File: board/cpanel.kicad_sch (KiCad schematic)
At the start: 12 parts, among them J18 LCD, SW11 RI, SW12 UP, SW13 LE, SW14 OK, SW15 DN, SW16 CANCEL, SW17 BACK, SW18 MENU, U19 BOB-12009, U20 MCP23008-xP

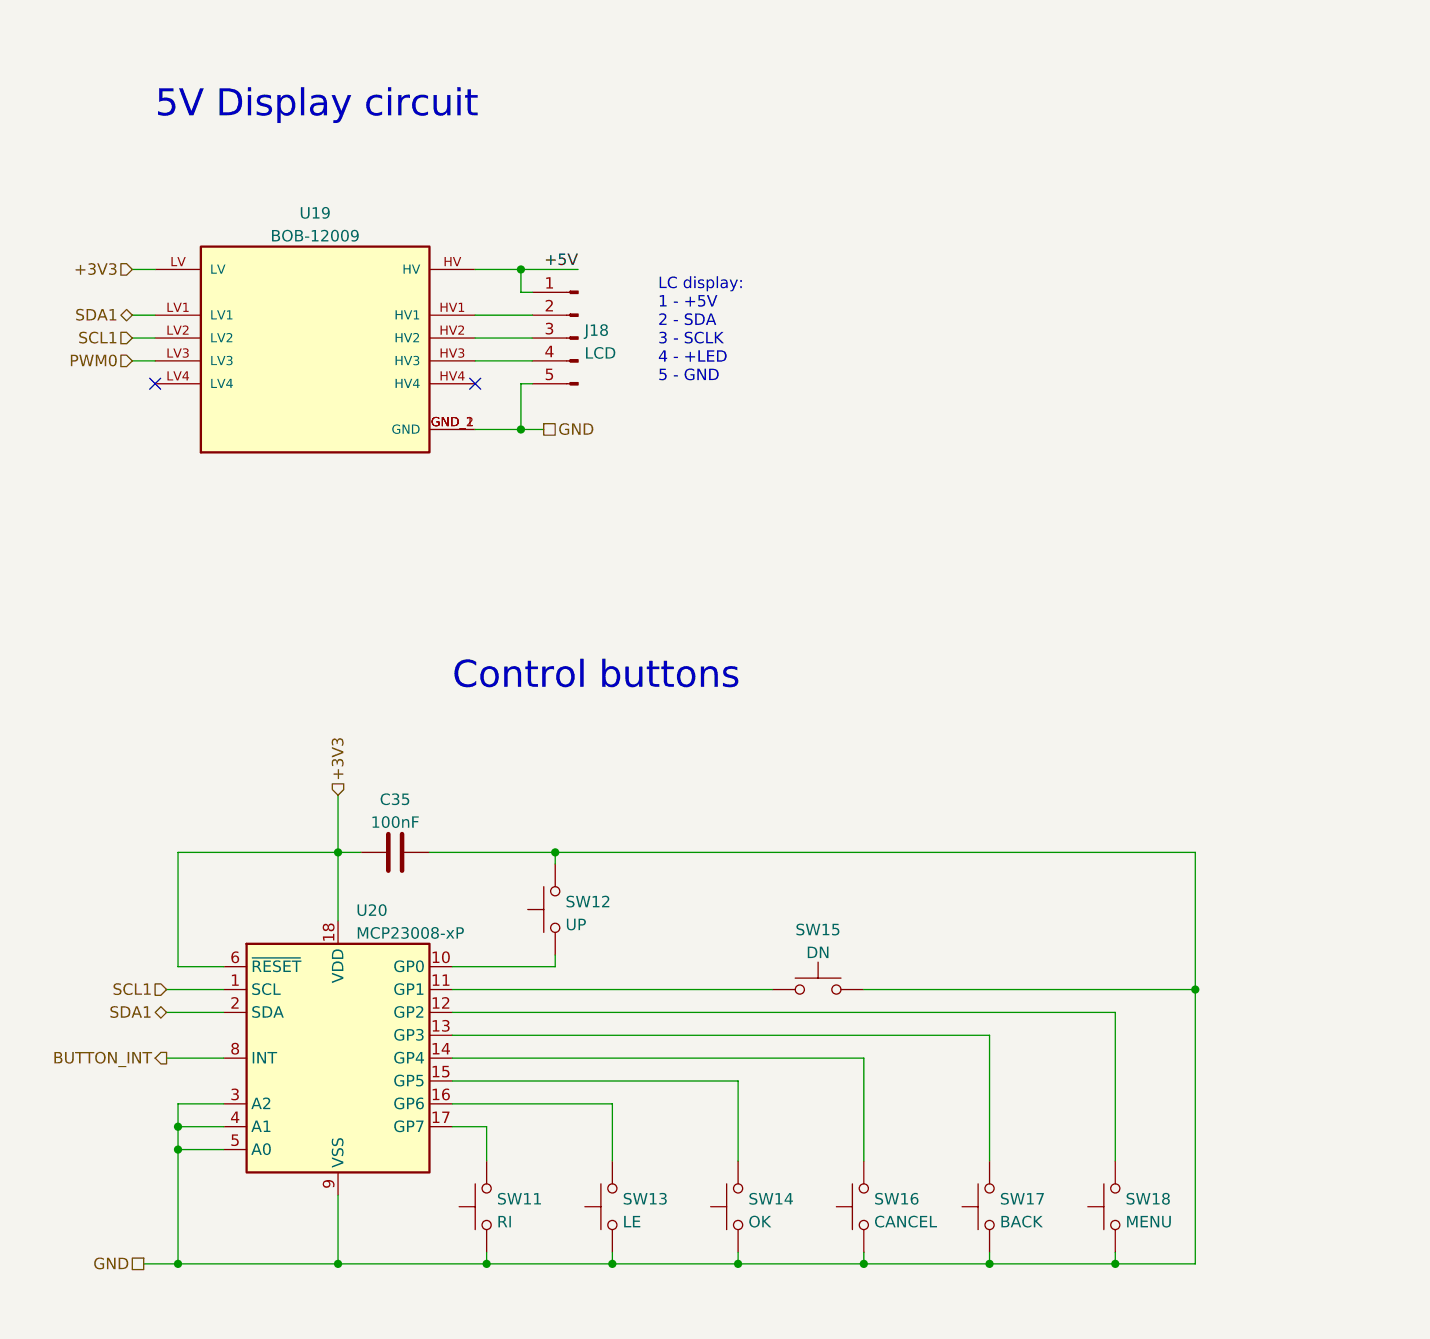
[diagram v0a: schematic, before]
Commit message: Modularize board.
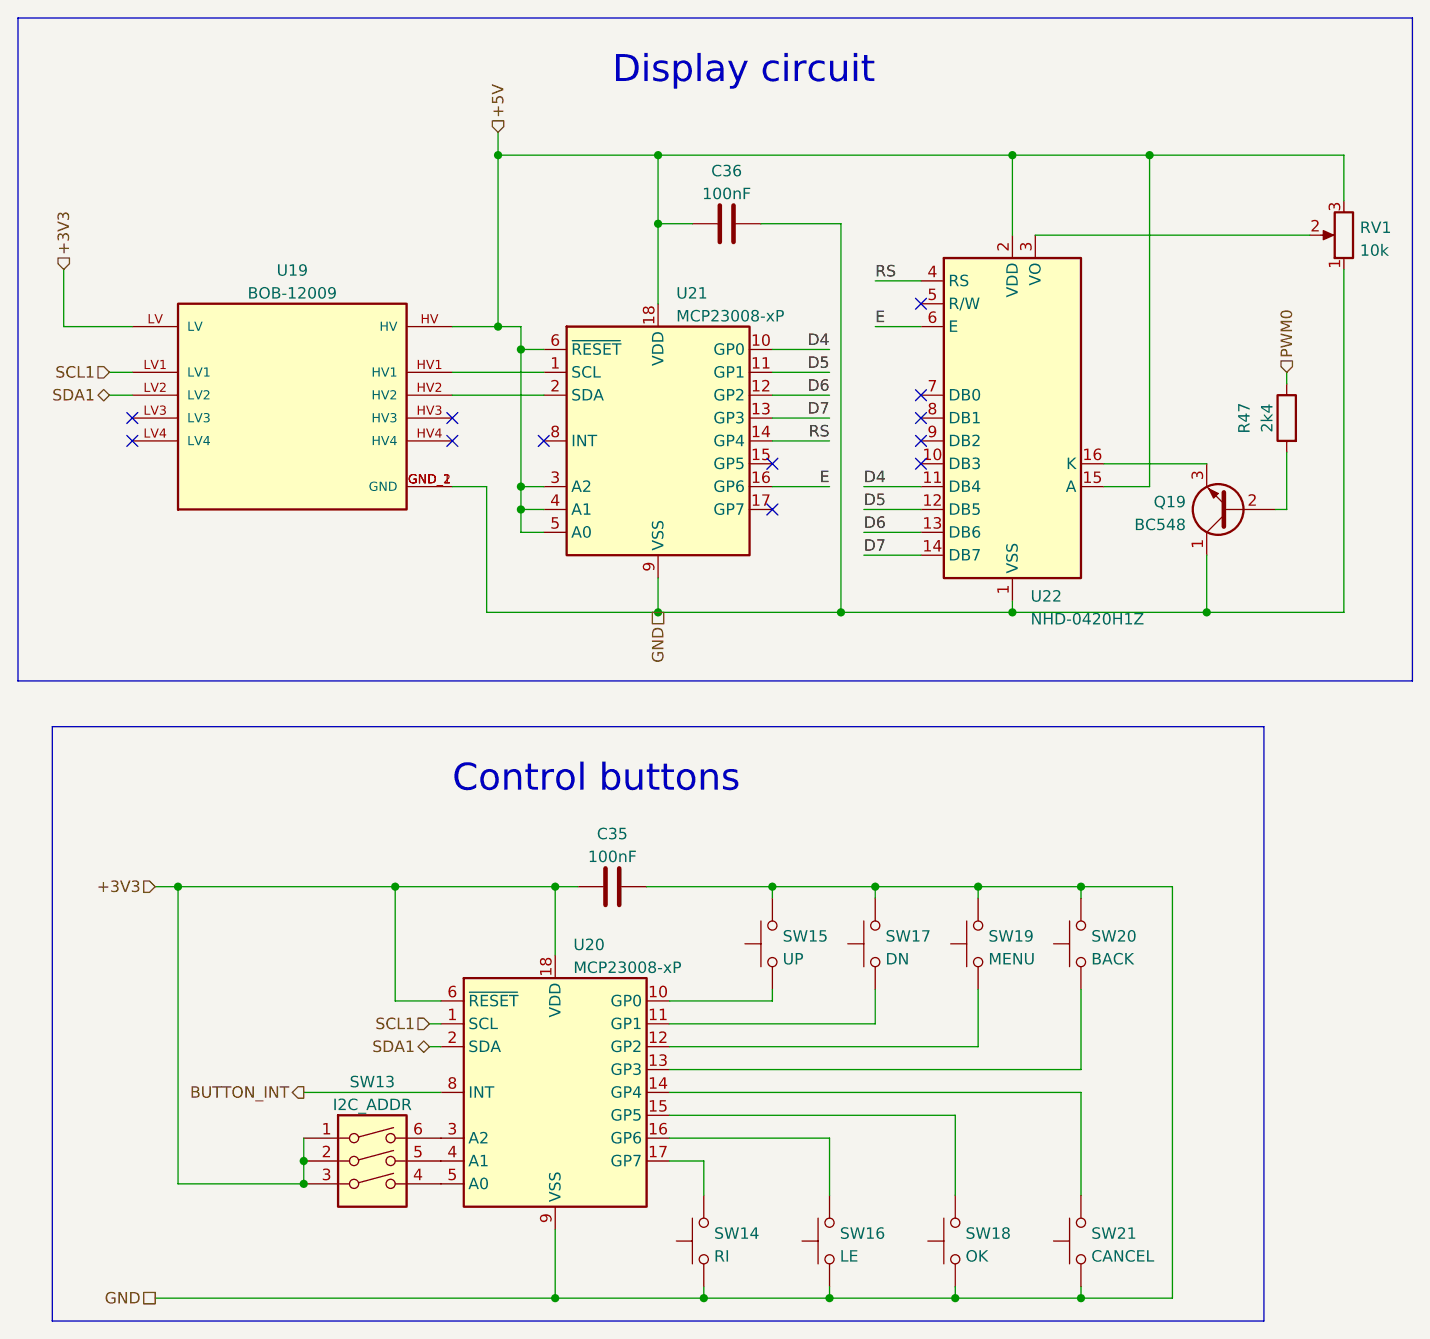
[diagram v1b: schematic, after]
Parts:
- removed J18: LCD, Connector_PinHeader_2.54mm:PinHeader_1x05_P2.54mm_Vertical, symbol Connector:Conn_01x05_Male
- added C36: 100nF, Capacitor_THT:C_Disc_D5.0mm_W2.5mm_P5.00mm, symbol Device:C
- added Q19: BC548, Package_TO_SOT_THT:TO-92_Inline, symbol Transistor_BJT:BC548
- added R47: 2k4, Resistor_THT:R_Axial_DIN0516_L15.5mm_D5.0mm_P7.62mm_Vertical, symbol Device:R
- added RV1: 10k, Potentiometer_THT:Potentiometer_Vishay_T7-YA_Single_Vertical, symbol Device:R_Potentiometer
- added SW13: I2C_ADDR, Button_Switch_THT:SW_DIP_SPSTx03_Slide_9.78x9.8mm_W7.62mm_P2.54mm, symbol Switch:SW_DIP_x03
- added U21: MCP23008-xP, Package_DIP:DIP-18_W7.62mm, symbol Interface_Expansion:MCP23008-xP
- added U22: NHD-0420H1Z, Display:NHD-0420H1Z, symbol Display_Character:NHD-0420H1Z
- renumbered SW11 to SW14, SW12 to SW15, SW13 to SW16, SW15 to SW17, SW14 to SW18, SW18 to SW19, SW17 to SW20, SW16 to SW21
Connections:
- net +3V3: now also SW13.1, SW13.2, SW13.3
- net +5V: now also C36.1, RV1.3, U21.18 (VDD), U21.3 (A2), U21.4 (A1), U21.5 (A0), U21.6 (~{RESET}), U22.15 (A), U22.2 (VDD)
- net GND: now also SW19.2, SW20.2, C36.2, Q19.1 (C), RV1.1, U21.9 (VSS), U22.1 (VSS); no longer SW19.1, SW20.1, U20.3 (A2), U20.4 (A1), U20.5 (A0)
- net PWM0: now also R47.1; no longer U19.LV3
- net SCL1: now also U19.LV1; no longer U19.LV2
- net SDA1: now also U19.LV2; no longer U19.LV1
- net at U20.13 (GP3): now also SW20.1; no longer SW20.2
- net at U20.12 (GP2): now also SW19.1; no longer SW19.2
- net at U19.HV1: now also U21.1 (SCL)
- net at U19.HV2: now also U21.2 (SDA)
- new net: SW13.4, U20.5 (A0)
- new net: SW13.5, U20.4 (A1)
- new net: SW13.6, U20.3 (A2)
- new net: Q19.3 (E), U22.16 (K)
- new net: RV1.2, U22.3 (VO)
- new net: Q19.2 (B), R47.2
- new net D4: U21.10 (GP0), U22.11 (DB4)
- new net D5: U21.11 (GP1), U22.12 (DB5)
- new net D6: U21.12 (GP2), U22.13 (DB6)
- new net D7: U21.13 (GP3), U22.14 (DB7)
- new net E: U21.16 (GP6), U22.6 (E)
- new net RS: U21.14 (GP4), U22.4 (RS)
- no-connect marks 2 -> 12
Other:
- note added: "Display circuit"
- note removed: "5V Display circuit"
- note removed: "LC display: 1 - +5V 2 - SDA 3 - SCLK 4 - +LED 5 - GND"
- company: (none) -> Dirk Gottschalk
- title: (none) -> The Ulysses Board
- moved on the sheet: C35, SW14, SW15, SW16, SW17, SW18, SW19, SW20, SW21, U19, U20
